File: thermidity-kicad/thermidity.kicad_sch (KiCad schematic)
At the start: 19 parts, among them J1 Battery, J2 Display, J3 ISP, U1 MCP1501-30, U2 ATmega328P, U3 TMP36, U4 HIH-5030

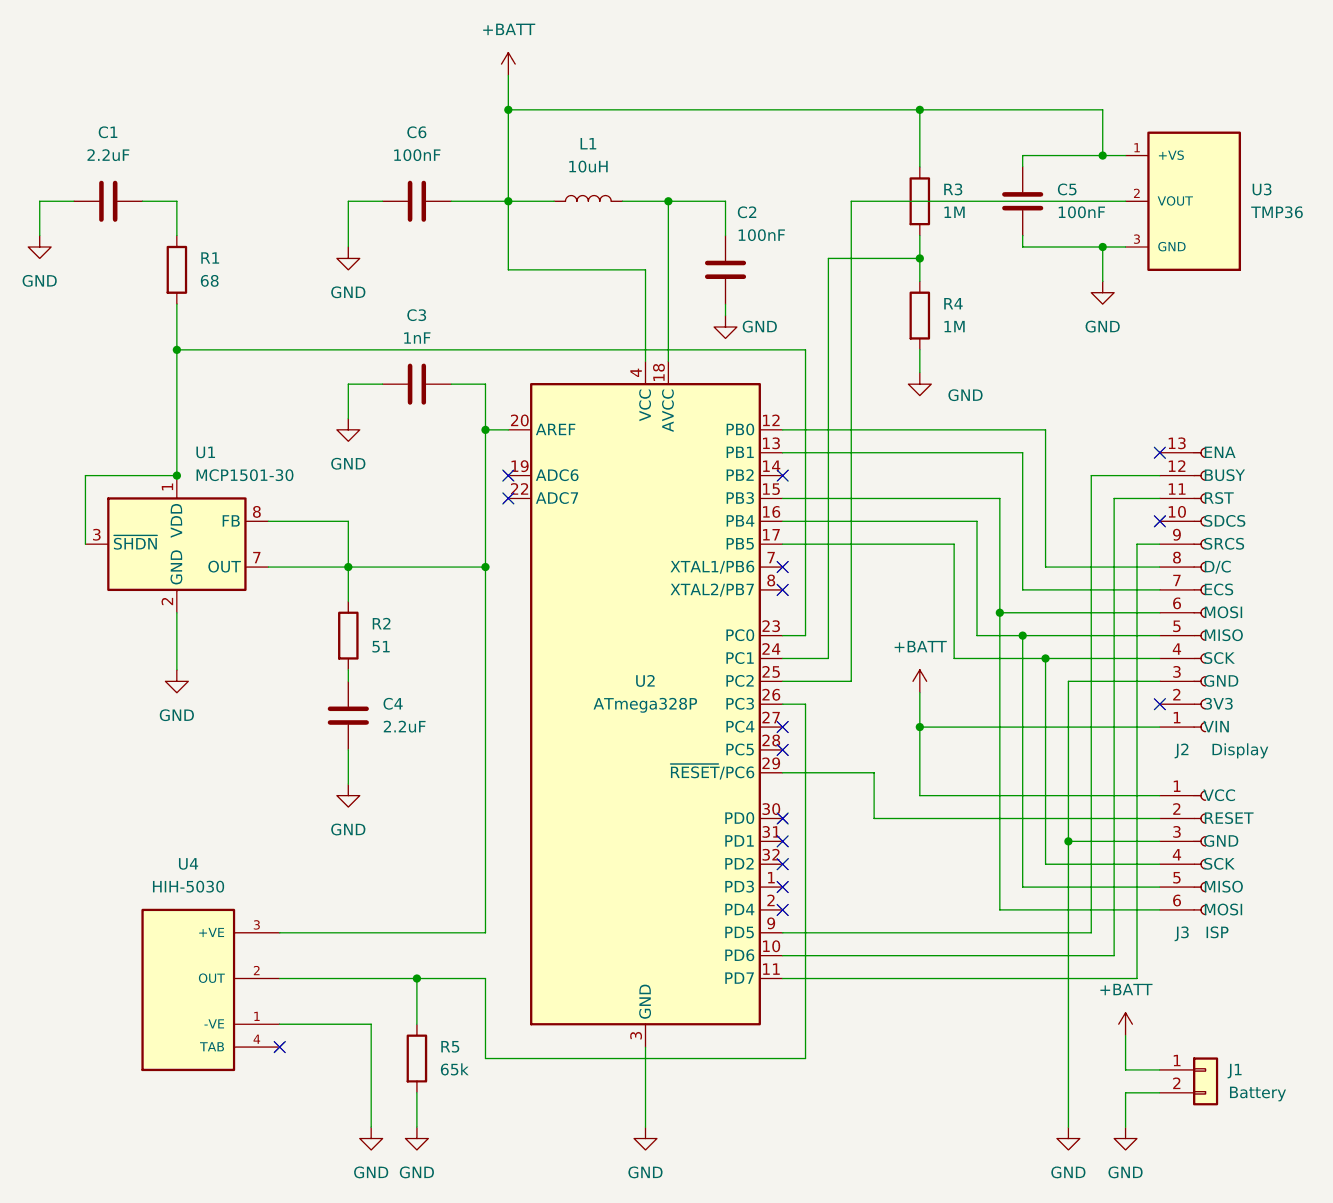
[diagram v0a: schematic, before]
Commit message: ratiometric measurement of humidity
- update schematic and README
- PCB not yet updated
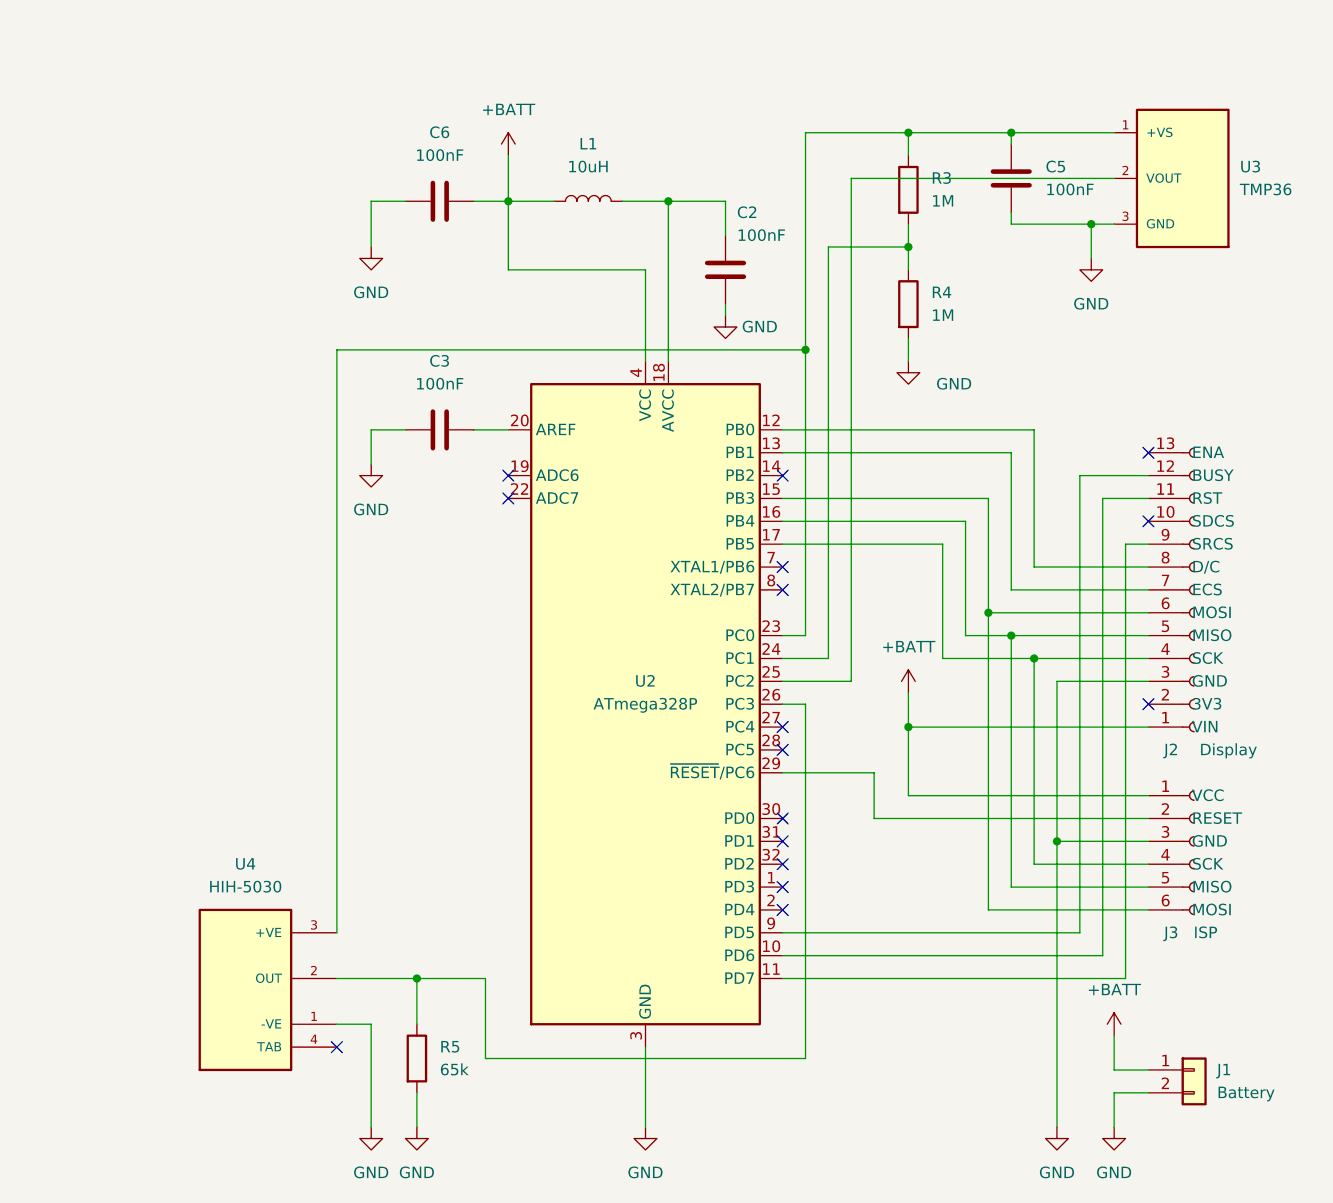
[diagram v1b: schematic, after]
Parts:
- removed C1, C4: 2.2uF, Capacitor_SMD:C_1206_3216Metric_Pad1.33x1.80mm_HandSolder, symbol Device:C
- removed R1: 68, Resistor_SMD:R_0805_2012Metric_Pad1.20x1.40mm_HandSolder, symbol Device:R
- removed R2: 51, Resistor_SMD:R_0805_2012Metric_Pad1.20x1.40mm_HandSolder, symbol Device:R
- removed U1: MCP1501-30, Package_SO:SOIC-8_3.9x4.9mm_P1.27mm, symbol Reference_Voltage:MCP1501-30xSN
- C3: value 1nF -> 100nF
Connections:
- net +BATT: no longer C5.1, R3.1, U3.1 (+VS)
- net at C3.2, U2.20 (AREF): no longer U4.3 (+VE)
- net at U2.23 (PC0): now also C5.1, R3.1, U3.1 (+VS), U4.3 (+VE)
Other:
- moved on the sheet: C3, C5, C6, J1, J2, J3, R3, R4, U3, U4

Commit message: ratiometric measurement of humidity
- update PCB
- measure battery voltage using internal 1.1V reference
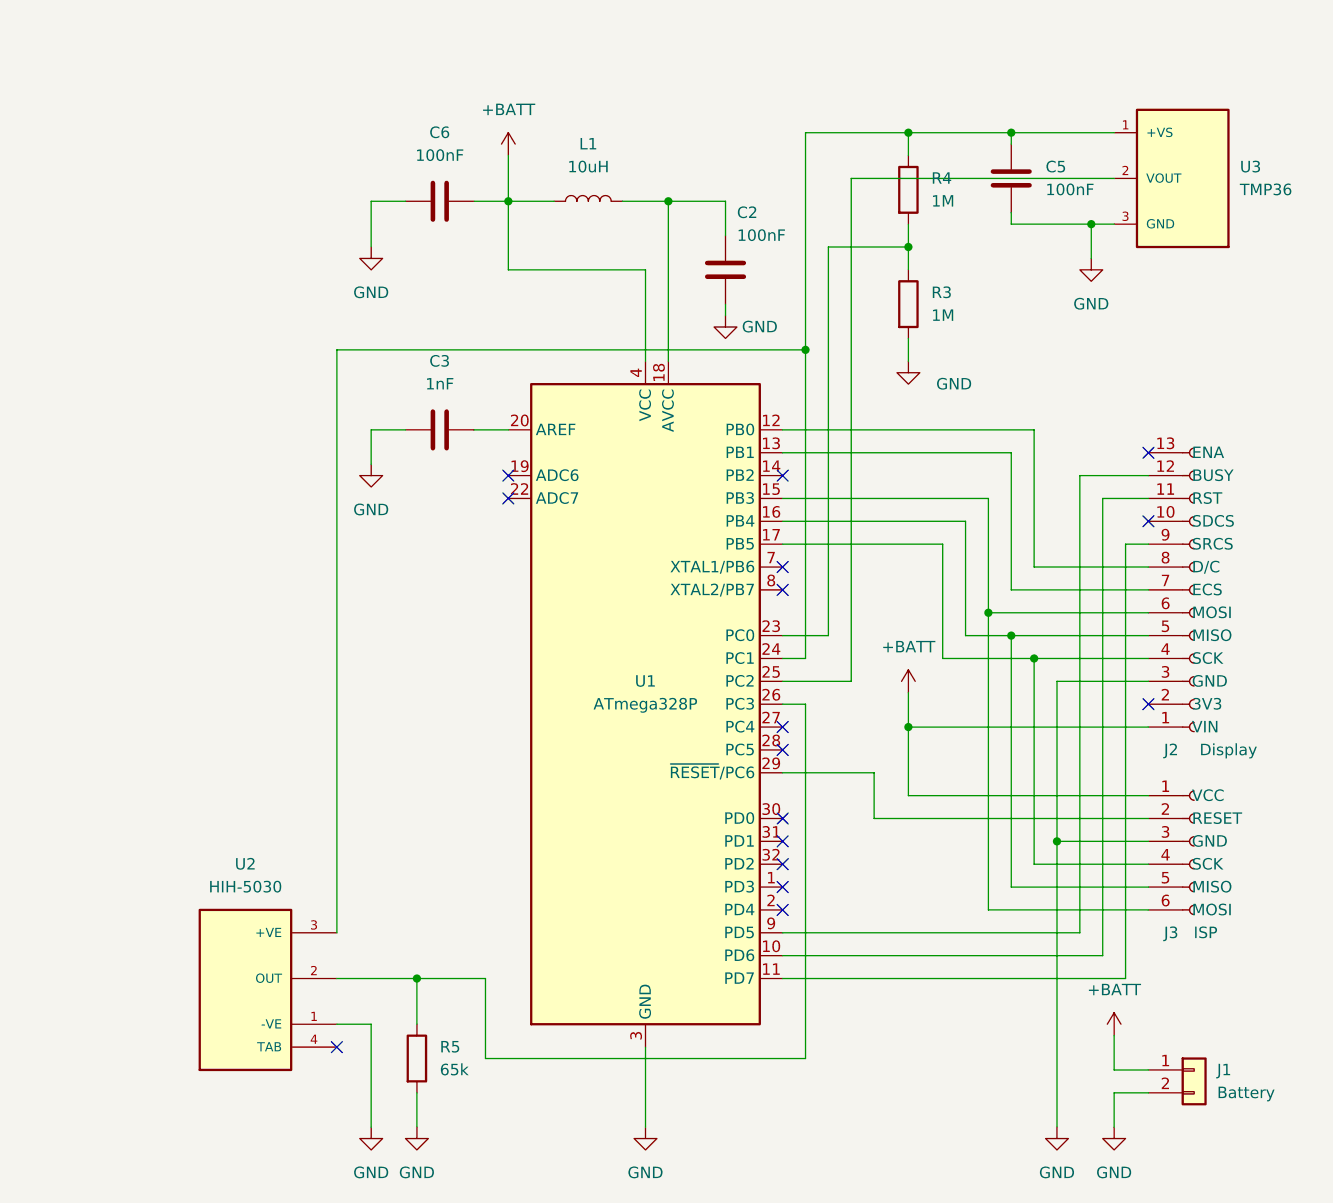
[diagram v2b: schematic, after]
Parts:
- C3: value 100nF -> 1nF
- renumbered R4 to R3, R3 to R4, U2 to U1, U4 to U2
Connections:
- net at C5.1, R4.1, U2.3 (+VE)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: now also U1.24 (PC1); no longer U1.23 (PC0)
- net at R3.1, R4.2: now also U1.23 (PC0); no longer U1.24 (PC1)
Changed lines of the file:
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@@
+    (stroke (width 0) (type default) (color 0 0 0 0))
+  )
+  (wire (pts (xy 163.83 91.44) (xy 161.29 91.44))
     (stroke (width 0) (type default) (color 0 0 0 0))
   )
@@
     (stroke (width 0) (type default) (color 0 0 0 0))
   )
-  (wire (pts (xy 166.37 91.44) (xy 161.29 91.44))
-    (stroke (width 0) (type default) (color 0 0 0 0))
-  )
   (wire (pts (xy 161.29 104.14) (xy 171.45 104.14))
     (stroke (width 0) (type default) (color 0 0 0 0))
@@
     (stroke (width 0) (type default) (color 0 0 0 0))
   )
-  (wire (pts (xy 166.37 45.72) (xy 166.37 91.44))
+  (wire (pts (xy 166.37 45.72) (xy 166.37 88.9))
     (stroke (width 0) (type default) (color 0 0 0 0))
   )
@@
     (stroke (width 0) (type default) (color 0 0 0 0))
   )
-  (wire (pts (xy 163.83 88.9) (xy 163.83 57.15))
+  (wire (pts (xy 163.83 57.15) (xy 163.83 91.44))
     (stroke (width 0) (type default) (color 0 0 0 0))
   )
@@
     (stroke (width 0) (type default) (color 0 0 0 0))
   )
+  (wire (pts (xy 161.29 88.9) (xy 166.37 88.9))
+    (stroke (width 0) (type default) (color 0 0 0 0))
+  )
   (wire (pts (xy 111.76 132.08) (xy 115.57 132.08))
     (stroke (width 0) (type default) (color 0 0 0 0))
@@
   )
   (wire (pts (xy 179.07 78.74) (xy 179.07 91.44))
-    (stroke (width 0) (type default) (color 0 0 0 0))
-  )
-  (wire (pts (xy 161.29 88.9) (xy 163.83 88.9))
     (stroke (width 0) (type default) (color 0 0 0 0))
   )
@@
   (symbol (lib_id "MCU_Microchip_ATmega:ATmega328P-A") (at 146.05 96.52 0) (unit 1)
     (in_bom yes) (on_board yes)
-    (property "Reference" "U2" (id 0) (at 146.05 93.98 0))
+    (property "Reference" "U1" (id 0) (at 146.05 93.98 0))
     (property "Value" "ATmega328P" (id 1) (at 146.05 96.52 0))
     (property "Footprint" "Package_QFP:TQFP-32_7x7mm_P0.8mm" (id 2) (at 146.05 96.52 0)
@@
   (symbol (lib_id "Device:R") (at 175.26 52.07 0) (unit 1)
     (in_bom yes) (on_board yes) (fields_autoplaced)
-    (property "Reference" "R4" (id 0) (at 177.8 50.7999 0)
+    (property "Reference" "R3" (id 0) (at 177.8 50.7999 0)
       (effects (font (size 1.27 1.27)) (justify left))
     )
@@
   (symbol (lib_id "HIH-5030-001:HIH-5030-001") (at 106.68 129.54 0) (unit 1)
     (in_bom yes) (on_board yes) (fields_autoplaced)
-    (property "Reference" "U4" (id 0) (at 101.6 114.3 0))
+    (property "Reference" "U2" (id 0) (at 101.6 114.3 0))
     (property "Value" "HIH-5030" (id 1) (at 101.6 116.84 0))
     (property "Footprint" "HIH-5030-001:HONEYWELL_HIH-5030-001" (id 2) (at 106.68 129.54 0)
@@
   (symbol (lib_id "Device:R") (at 175.26 39.37 0) (unit 1)
     (in_bom yes) (on_board yes) (fields_autoplaced)
-    (property "Reference" "R3" (id 0) (at 177.8 38.0999 0)
+    (property "Reference" "R4" (id 0) (at 177.8 38.0999 0)
       (effects (font (size 1.27 1.27)) (justify left))
     )
@@
     (in_bom yes) (on_board yes) (fields_autoplaced)
     (property "Reference" "C3" (id 0) (at 123.19 58.42 90))
-    (property "Value" "100nF" (id 1) (at 123.19 60.96 90))
+    (property "Value" "1nF" (id 1) (at 123.19 60.96 90))
     (property "Footprint" "Capacitor_SMD:C_1206_3216Metric_Pad1.33x1.80mm_HandSolder" (id 2) (at 127 65.0748 0)
       (effects (font (size 1.27 1.27)) hide)
@@
     )
     (path "/fb41d1b8-7978-4471-8222-322ad33b566c"
-      (reference "C3") (unit 1) (value "100nF") (footprint "Capacitor_SMD:C_1206_3216Metric_Pad1.33x1.80mm_HandSolder")
+      (reference "C3") (unit 1) (value "1nF") (footprint "Capacitor_SMD:C_1206_3216Metric_Pad1.33x1.80mm_HandSolder")
     )
     (path "/0178a398-4cac-462d-a5f8-54e853b1fa89"
@@
       (reference "L1") (unit 1) (value "10uH") (footprint "Inductor_SMD:L_1210_3225Metric_Pad1.42x2.65mm_HandSolder")
     )
+    (path "/d690645f-ce9c-4e4e-9a40-30e90181925c"
+      (reference "R3") (unit 1) (value "1M") (footprint "Resistor_SMD:R_0805_2012Metric_Pad1.20x1.40mm_HandSolder")
+    )
     (path "/f5367a98-6a53-432b-8730-086e1bb8663c"
-      (reference "R3") (unit 1) (value "1M") (footprint "Resistor_SMD:R_0805_2012Metric_Pad1.20x1.40mm_HandSolder")
-    )
-    (path "/d690645f-ce9c-4e4e-9a40-30e90181925c"
       (reference "R4") (unit 1) (value "1M") (footprint "Resistor_SMD:R_0805_2012Metric_Pad1.20x1.40mm_HandSolder")
     )
@@
     )
     (path "/a564f624-0149-43d3-9b25-20abc178b1e7"
-      (reference "U2") (unit 1) (value "ATmega328P") (footprint "Package_QFP:TQFP-32_7x7mm_P0.8mm")
+      (reference "U1") (unit 1) (value "ATmega328P") (footprint "Package_QFP:TQFP-32_7x7mm_P0.8mm")
+    )
+    (path "/e6831fa3-d0e2-442b-bad0-235e2cccce1e"
+      (reference "U2") (unit 1) (value "HIH-5030") (footprint "HIH-5030-001:HONEYWELL_HIH-5030-001")
     )
     (path "/d57ede9f-d6ce-400c-b2ec-0a0c742662bf"
       (reference "U3") (unit 1) (value "TMP36") (footprint "TMP36GT9:XDCR_TMP36GT9")
     )
-    (path "/e6831fa3-d0e2-442b-bad0-235e2cccce1e"
-      (reference "U4") (unit 1) (value "HIH-5030") (footprint "HIH-5030-001:HONEYWELL_HIH-5030-001")
-    )
-  )
+  )
